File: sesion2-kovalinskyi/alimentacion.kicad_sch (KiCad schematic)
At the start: 4 parts, among them J1 Screw_Terminal_01x02, U1 LD1117S33TR_SOT223

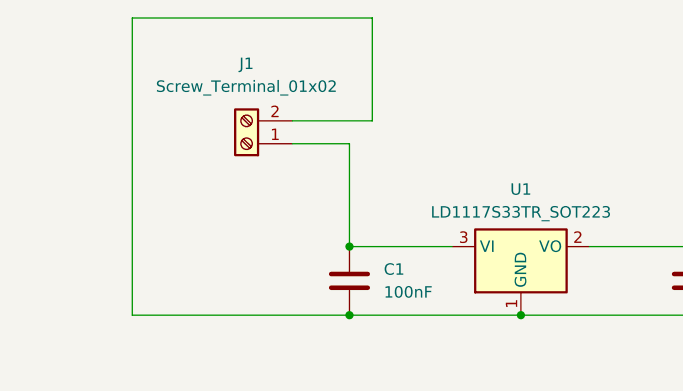
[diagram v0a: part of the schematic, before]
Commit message: Etapa de MCU completada
- MCU
- filtros RC
- resolución ERC con PWR_FLAG
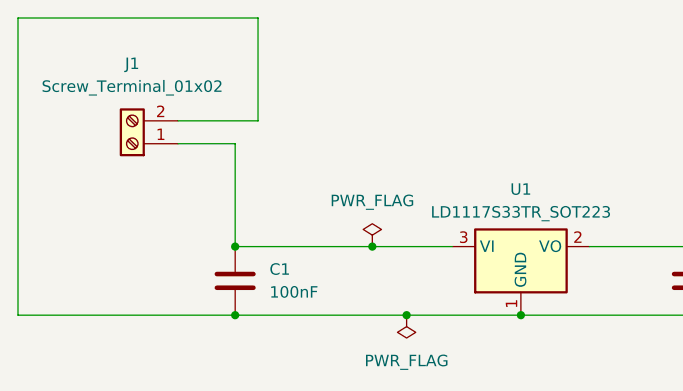
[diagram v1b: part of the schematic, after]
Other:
- moved on the sheet: C1, J1
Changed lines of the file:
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@@
 	(paper "A4")
+	(junction
+		(at 85.09 74.93)
+		(diameter 0)
+		(color 0 0 0 0)
+	)
 	(junction
 		(at 120.65 82.55)
@@
 	)
 	(junction
+		(at 88.9 82.55)
+		(diameter 0)
+		(color 0 0 0 0)
+	)
+	(junction
 		(at 120.65 74.93)
 		(diameter 0)
@@
 	)
 	(junction
-		(at 82.55 74.93)
+		(at 69.85 74.93)
 		(diameter 0)
 		(color 0 0 0 0)
 	)
 	(junction
-		(at 82.55 82.55)
+		(at 69.85 82.55)
 		(diameter 0)
 		(color 0 0 0 0)
@@
 	(wire
 		(pts
-			(xy 58.42 82.55) (xy 82.55 82.55)
-		)
-		(stroke
-			(width 0)
-			(type default)
-		)
-	)
-	(wire
-		(pts
-			(xy 58.42 49.53) (xy 58.42 82.55)
-		)
-		(stroke
-			(width 0)
-			(type default)
-		)
-	)
-	(wire
-		(pts
-			(xy 85.09 49.53) (xy 58.42 49.53)
+			(xy 45.72 82.55) (xy 69.85 82.55)
+		)
+		(stroke
+			(width 0)
+			(type default)
+		)
+	)
+	(wire
+		(pts
+			(xy 45.72 49.53) (xy 45.72 82.55)
+		)
+		(stroke
+			(width 0)
+			(type default)
+		)
+	)
+	(wire
+		(pts
+			(xy 72.39 49.53) (xy 45.72 49.53)
 		)
 		(stroke
@@
 	(wire
 		(pts
-			(xy 82.55 82.55) (xy 101.6 82.55)
+			(xy 69.85 82.55) (xy 88.9 82.55)
 		)
 		(stroke
@@
 	(wire
 		(pts
-			(xy 82.55 63.5) (xy 82.55 74.93)
-		)
-		(stroke
-			(width 0)
-			(type default)
-		)
-	)
-	(wire
-		(pts
-			(xy 85.09 60.96) (xy 85.09 49.53)
-		)
-		(stroke
-			(width 0)
-			(type default)
-		)
-	)
-	(wire
-		(pts
-			(xy 82.55 74.93) (xy 93.98 74.93)
+			(xy 69.85 63.5) (xy 69.85 74.93)
+		)
+		(stroke
+			(width 0)
+			(type default)
+		)
+	)
+	(wire
+		(pts
+			(xy 88.9 82.55) (xy 101.6 82.55)
+		)
+		(stroke
+			(width 0)
+			(type default)
+		)
+	)
+	(wire
+		(pts
+			(xy 72.39 60.96) (xy 72.39 49.53)
+		)
+		(stroke
+			(width 0)
+			(type default)
+		)
+	)
+	(wire
+		(pts
+			(xy 69.85 74.93) (xy 93.98 74.93)
 		)
 		(stroke
@@
 	(wire
 		(pts
-			(xy 76.2 60.96) (xy 85.09 60.96)
-		)
-		(stroke
-			(width 0)
-			(type default)
-		)
-	)
-	(wire
-		(pts
-			(xy 82.55 63.5) (xy 76.2 63.5)
+			(xy 63.5 60.96) (xy 72.39 60.96)
+		)
+		(stroke
+			(width 0)
+			(type default)
+		)
+	)
+	(wire
+		(pts
+			(xy 69.85 63.5) (xy 63.5 63.5)
 		)
 		(stroke
@@
 	(symbol
 		(lib_id "Connector:Screw_Terminal_01x02")
-		(at 71.12 63.5 180)
+		(at 58.42 63.5 180)
 		(unit 1)
 		(body_style 1)
@@
 		(fields_autoplaced yes)
 		(property "Reference" "J1"
-			(at 71.12 54.61 0)
+			(at 58.42 54.61 0)
 			(show_name no)
 			(do_not_autoplace no)
@@
 		)
 		(property "Value" "Screw_Terminal_01x02"
-			(at 71.12 57.15 0)
+			(at 58.42 57.15 0)
 			(show_name no)
 			(do_not_autoplace no)
@@
 		)
 		(property "Footprint" "TerminalBlock_Phoenix:TerminalBlock_Phoenix_MPT-0,5-2-2.54_1x02_P2.54mm_Horizontal"
-			(at 71.12 63.5 0)
+			(at 58.42 63.5 0)
 			(hide yes)
 			(show_name no)
@@
 		)
 		(property "Datasheet" ""
-			(at 71.12 63.5 0)
+			(at 58.42 63.5 0)
 			(hide yes)
 			(show_name no)
@@
 		)
 		(property "Description" "Generic screw terminal, single row, 01x02, script generated (kicad-library-utils/schlib/autogen/connector/)"
-			(at 71.12 63.5 0)
+			(at 58.42 63.5 0)
 			(hide yes)
 			(show_name no)
@@
 		)
 		(property "MPN" "1725656"
-			(at 71.12 63.5 0)
+			(at 58.42 63.5 0)
 			(hide yes)
 			(show_name no)
@@
 	)
 	(symbol
+		(lib_id "power:PWR_FLAG")
+		(at 88.9 82.55 180)
+		(unit 1)
+		(body_style 1)
+		(exclude_from_sim no)
+		(in_bom yes)
+		(on_board yes)
+		(in_pos_files yes)
+		(dnp no)
+		(fields_autoplaced yes)
+		(property "Reference" "#FLG02"
+			(at 88.9 84.455 0)
+			(hide yes)
+			(show_name no)
+			(do_not_autoplace no)
+			(effects
+				(font
+					(size 1.27 1.27)
+				)
+			)
+		)
+		(property "Value" "PWR_FLAG"
+			(at 88.9 87.63 0)
+			(show_name no)
+			(do_not_autoplace no)
+			(effects
+				(font
+					(size 1.27 1.27)
+				)
+			)
+		)
+		(property "Footprint" ""
+			(at 88.9 82.55 0)
+			(hide yes)
+			(show_name no)
+			(do_not_autoplace no)
+			(effects
+				(font
+					(size 1.27 1.27)
+				)
+			)
+		)
+		(property "Datasheet" ""
+			(at 88.9 82.55 0)
+			(hide yes)
+			(show_name no)
+			(do_not_autoplace no)
+			(effects
+				(font
+					(size 1.27 1.27)
+				)
+			)
+		)
+		(property "Description" "Special symbol for telling ERC where power comes from"
+			(at 88.9 82.55 0)
+			(hide yes)
+			(show_name no)
+			(do_not_autoplace no)
+			(effects
+				(font
+					(size 1.27 1.27)
+				)
+			)
+		)
+		(pin "1"
+		)
+		(instances
+			(project "sesion2-kovalinskyi"
+				(path "/99d4a334-3c53-424d-bcc9-9b696a6ef66c/f5ed50df-eccc-4114-bd29-75cb10e7f4d7"
+					(reference "#FLG02")
+					(unit 1)
+				)
+			)
+		)
+	)
+	(symbol
 		(lib_id "Device:C")
 		(at 120.65 78.74 180)
@@
 	)
 	(symbol
+		(lib_id "power:PWR_FLAG")
+		(at 85.09 74.93 0)
+		(unit 1)
+		(body_style 1)
+		(exclude_from_sim no)
+		(in_bom yes)
+		(on_board yes)
+		(in_pos_files yes)
+		(dnp no)
+		(fields_autoplaced yes)
+		(property "Reference" "#FLG01"
+			(at 85.09 73.025 0)
+			(hide yes)
+			(show_name no)
+			(do_not_autoplace no)
+			(effects
+				(font
+					(size 1.27 1.27)
+				)
+			)
+		)
+		(property "Value" "PWR_FLAG"
+			(at 85.09 69.85 0)
+			(show_name no)
+			(do_not_autoplace no)
+			(effects
+				(font
+					(size 1.27 1.27)
+				)
+			)
+		)
+		(property "Footprint" ""
+			(at 85.09 74.93 0)
+			(hide yes)
+			(show_name no)
+			(do_not_autoplace no)
+			(effects
+				(font
+					(size 1.27 1.27)
+				)
+			)
+		)
+		(property "Datasheet" ""
+			(at 85.09 74.93 0)
+			(hide yes)
+			(show_name no)
+			(do_not_autoplace no)
+			(effects
+				(font
+					(size 1.27 1.27)
+				)
+			)
+		)
+		(property "Description" "Special symbol for telling ERC where power comes from"
+			(at 85.09 74.93 0)
+			(hide yes)
+			(show_name no)
+			(do_not_autoplace no)
+			(effects
+				(font
+					(size 1.27 1.27)
+				)
+			)
+		)
+		(pin "1"
+		)
+		(instances
+			(project "sesion2-kovalinskyi"
+				(path "/99d4a334-3c53-424d-bcc9-9b696a6ef66c/f5ed50df-eccc-4114-bd29-75cb10e7f4d7"
+					(reference "#FLG01")
+					(unit 1)
+				)
+			)
+		)
+	)
+	(symbol
 		(lib_id "Device:C")
-		(at 82.55 78.74 180)
+		(at 69.85 78.74 180)
 		(unit 1)
 		(body_style 1)
@@
 		(fields_autoplaced yes)
 		(property "Reference" "C1"
-			(at 86.36 77.4699 0)
+			(at 73.66 77.4699 0)
 			(show_name no)
 			(do_not_autoplace no)
@@
 		)
 		(property "Value" "100nF"
-			(at 86.36 80.0099 0)
+			(at 73.66 80.0099 0)
 			(show_name no)
 			(do_not_autoplace no)
@@
 		)
 		(property "Footprint" "Capacitor_SMD:C_0805_2012Metric"
-			(at 81.5848 74.93 0)
+			(at 68.8848 74.93 0)
 			(hide yes)
 			(show_name no)
@@
 		)
 		(property "Datasheet" ""
-			(at 82.55 78.74 0)
+			(at 69.85 78.74 0)
 			(hide yes)
 			(show_name no)
@@
 		)
 		(property "Description" "Unpolarized capacitor"
-			(at 82.55 78.74 0)
-			(hide yes)
-			(show_name no)
+			(at 69.85 78.74 0)
+			(hide yes)
+			(show_name no)

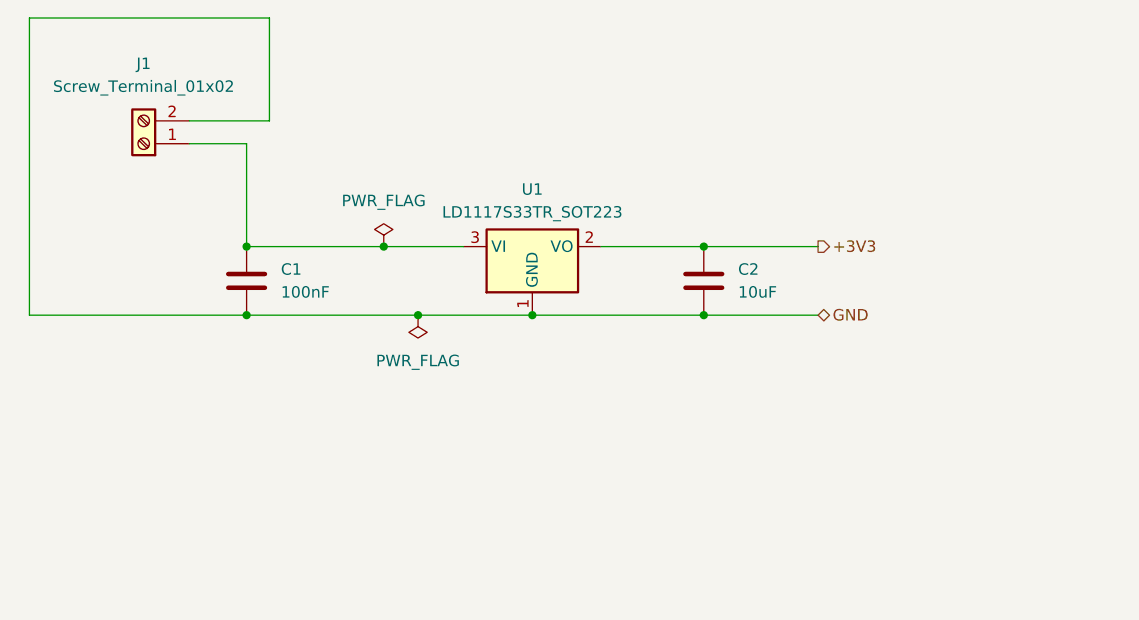
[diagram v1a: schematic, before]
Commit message: Avance en layout y enrutado preliminar
- Enrutadas señales de datos, filtros y componentes pasivos.
- Implementados condensadores de desacoplo y test points (VIN, 3V3, GND).

Pendiente:
- Corregir asignación de ancho para pistas de alimentación (+3V3 a 0,5 mm).
- Validar conexiones a GND y cosido de vías con el plano inferior (B.Cu).
- Ejecutar DRC final y recálculo de zonas de relleno.
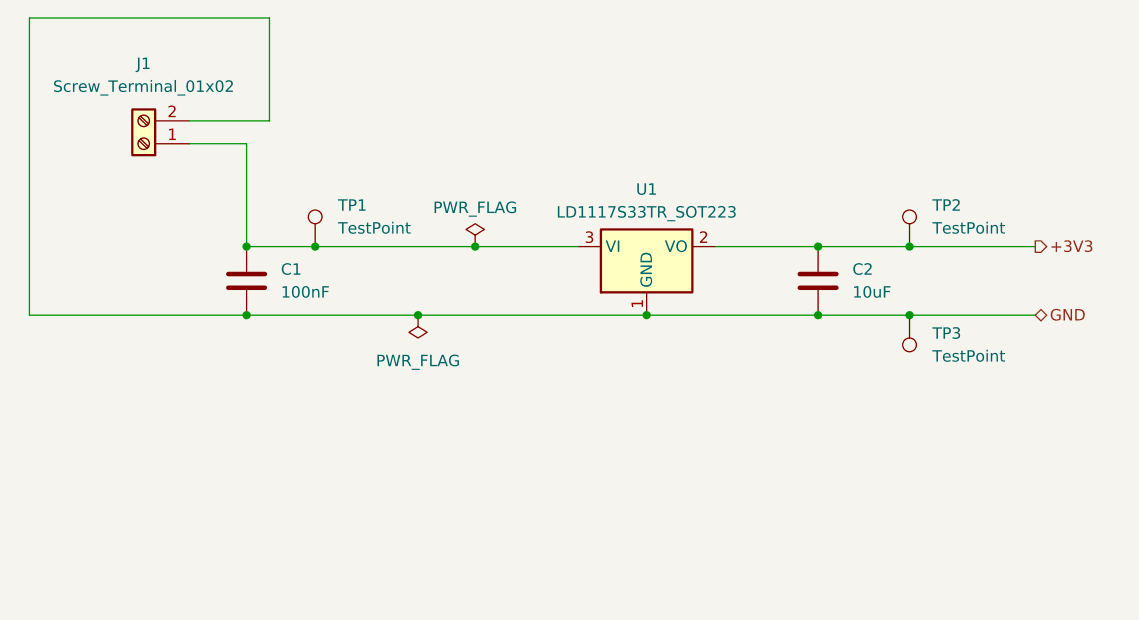
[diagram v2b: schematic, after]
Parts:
- added TP1, TP2, TP3: TestPoint, TestPoint:TestPoint_Pad_D1.5mm, symbol Connector:TestPoint
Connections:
- net +3V3: now also TP2.1
- net GND: now also TP3.1
- net at C1.2, J1.1 (Pin_1), U1.3 (VI): now also TP1.1
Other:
- moved on the sheet: C2, U1

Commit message: Calculo de impedancia y enrutado SPI e I2C
- I2C enrutado en Capa 3 (Stripline) con meandros (regla 3W) y desacoplo C8 pegado a los pines.
- SPI en Capa 1 con ajuste de longitud en SCK, MOSI y MISO (~25,35 mm) y puente en Capa 3 para SPI_CS.
- Validada la integridad de señal en los buses; líneas de datos libres de errores DRC.
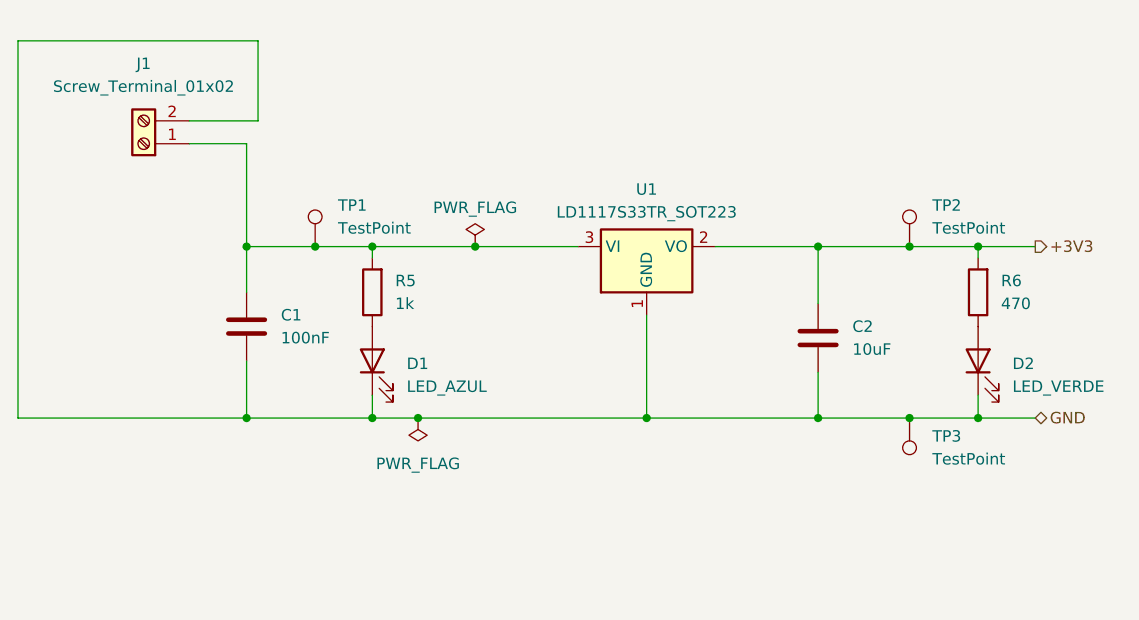
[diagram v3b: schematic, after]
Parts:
- added D1: LED_AZUL, LED_SMD:LED_0805_2012Metric, symbol Device:LED
- added D2: LED_VERDE, LED_SMD:LED_0805_2012Metric, symbol Device:LED
- added R5: 1k, Resistor_SMD:R_0805_2012Metric, symbol Device:R
- added R6: 470, Resistor_SMD:R_0805_2012Metric, symbol Device:R
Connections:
- net +3V3: now also R6.2
- net GND: now also D1.1 (K), D2.1 (K)
- net at C1.2, J1.1 (Pin_1), TP1.1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: now also R5.2
- new net: D1.2 (A), R5.1
- new net: D2.2 (A), R6.1
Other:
- moved on the sheet: C1, C2, TP3

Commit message: Apartados 1 - 3 completados; integrando protecciones (apartado 4) en el esquemático
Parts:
- added D3: D_TVS, Diode_SMD:D_SOD-123, symbol Device:D_TVS
- added FB1: 100 Ohm @ 100MHz, Resistor_SMD:R_0805_2012Metric, symbol Device:FerriteBead_Small
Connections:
- net GND: now also D3.2 (A2)
- net at C1.2, R5.2, TP1.1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: now also FB1.2; no longer J1.1 (Pin_1)
- new net: D3.1 (A1), FB1.1, J1.1 (Pin_1)
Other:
- moved on the sheet: C1, C2, D1, D2, R5, R6, TP1, TP2, TP3, U1

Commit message: Copia de seguridad Sesión 5
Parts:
- C1: MPN (none) -> CC0805KRX7R9BB104
- C2: MPN (none) -> CC0805MKX5R7BB106
- D1: MPN (none) -> 150080BS75000
- D2: MPN (none) -> 150080VS75000
- D3: MPN (none) -> PESD3V3L1BA
- FB1: MPN (none) -> BLM21PG221SN1D
- R5: MPN (none) -> RC0805FR-071KL
- R6: MPN (none) -> RC0805FR-07470RL
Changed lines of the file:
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@@
+			)
+		)
+		(property "MPN" "BLM21PG221SN1D"
+			(at 69.85 78.74 0)
+			(hide yes)
+			(show_name no)
+			(do_not_autoplace no)
+			(effects
+				(font
+					(size 1.27 1.27)
+				)
 			)
 		)
@@
 			)
 		)
+		(property "MPN" "150080BS75000"
+			(at 83.82 101.6 90)
+			(hide yes)
+			(show_name no)
+			(do_not_autoplace no)
+			(effects
+				(font
+					(size 1.27 1.27)
+				)
+			)
+		)
 		(pin "1"
 		)
@@
 			)
 		)
+		(property "MPN" "RC0805FR-07470RL"
+			(at 151.13 93.98 0)
+			(hide yes)
+			(show_name no)
+			(do_not_autoplace no)
+			(effects
+				(font
+					(size 1.27 1.27)
+				)
+			)
+		)
 		(pin "1"
 		)
@@
 			)
 		)
+		(property "MPN" "150080VS75000"
+			(at 151.13 101.6 90)
+			(hide yes)
+			(show_name no)
+			(do_not_autoplace no)
+			(effects
+				(font
+					(size 1.27 1.27)
+				)
+			)
+		)
 		(pin "1"
 		)
@@
 			)
 		)
+		(property "MPN" "CC0805MKX5R7BB106"
+			(at 133.35 99.06 0)
+			(hide yes)
+			(show_name no)
+			(do_not_autoplace no)
+			(effects
+				(font
+					(size 1.27 1.27)
+				)
+			)
+		)
 		(pin "2"
 		)
@@
 			)
 		)
+		(property "MPN" "PESD3V3L1BA"
+			(at 74.93 62.23 90)
+			(hide yes)
+			(show_name no)
+			(do_not_autoplace no)
+			(effects
+				(font
+					(size 1.27 1.27)
+				)
+			)
+		)
 		(pin "2"
 		)
@@
 			)
 		)
+		(property "MPN" "CC0805KRX7R9BB104"
+			(at 69.85 97.79 0)
+			(hide yes)
+			(show_name no)
+			(do_not_autoplace no)
+			(effects
+				(font
+					(size 1.27 1.27)
+				)
+			)
+		)
 		(pin "2"
 		)
@@
 			(at 83.82 93.98 0)
 			(hide yes)
+			(show_name no)
+			(do_not_autoplace no)
+			(effects
+				(font
+					(size 1.27 1.27)
+				)
+			)
+		)
+		(property "MPN" "RC0805FR-071KL"
+			(at 83.82 93.98 0)
+			(hide yes)
